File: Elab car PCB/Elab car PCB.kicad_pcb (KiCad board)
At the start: 2 copper layers, 0 parts

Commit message: PCB creation
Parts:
- added C1: 20pF, Capacitor_SMD:C_1206_3216Metric_Pad1.33x1.80mm_HandSolder, F.Cu at (182.2, 73.7)
- added C2: 20pF, Capacitor_SMD:C_1206_3216Metric_Pad1.33x1.80mm_HandSolder, F.Cu at (193.7, 73.7)
- added C3: 10µF, Capacitor_SMD:CP_Elec_5x4.5, F.Cu at (114.9, 89.5)
- added C4: 22µF, Capacitor_SMD:CP_Elec_5x5.3, F.Cu at (94.6, 89.5)
- added C5: 47µF, Capacitor_SMD:CP_Elec_6.3x5.8, F.Cu at (104.1, 130.2)
- added C6: 10µF, Capacitor_SMD:CP_Elec_5x4.5, F.Cu at (104.5, 105.4)
- added C7: 100nF, Capacitor_SMD:C_1206_3216Metric_Pad1.33x1.80mm_HandSolder, F.Cu at (121.3, 51.8)
- added D1: D_Schottky, Diode_SMD:D_1206_3216Metric_Pad1.42x1.75mm_HandSolder, F.Cu at (183.5, 101.0)
- added D10: D_Schottky, Diode_SMD:D_1206_3216Metric_Pad1.42x1.75mm_HandSolder, F.Cu at (163.0, 89.7)
- added D11: WS2812B, LED_SMD:LED_WS2812B_PLCC4_5.0x5.0mm_P3.2mm, F.Cu at (95.5, 61.3)
- added D12: WS2812B, LED_SMD:LED_WS2812B_PLCC4_5.0x5.0mm_P3.2mm, F.Cu at (95.5, 141.9)
- added D13: WS2812B, LED_SMD:LED_WS2812B_PLCC4_5.0x5.0mm_P3.2mm, F.Cu at (183.9, 141.9)
- added D14: WS2812B, LED_SMD:LED_WS2812B_PLCC4_5.0x5.0mm_P3.2mm, F.Cu at (183.9, 61.3)
- added D15: Blue_led, LED_SMD:LED_0805_2012Metric_Pad1.15x1.40mm_HandSolder, F.Cu at (137.8, 73.4)
- added D16: D_Schottky, Diode_SMD:D_1206_3216Metric_Pad1.42x1.75mm_HandSolder, F.Cu at (113.7, 116.8)
- added D17: 3.3V PWR, LED_SMD:LED_0805_2012Metric_Pad1.15x1.40mm_HandSolder, F.Cu at (85.0, 98.0)
- added D18: D_Schottky, Diode_SMD:D_1206_3216Metric_Pad1.42x1.75mm_HandSolder, F.Cu at (112.4, 111.8)
- added D19: 5V PWR, LED_SMD:LED_0805_2012Metric_Pad1.15x1.40mm_HandSolder, F.Cu at (85.0, 105.0)
- added D2: D_Schottky, Diode_SMD:D_1206_3216Metric_Pad1.42x1.75mm_HandSolder, F.Cu at (112.8, 121.9)
- added D20: D_Schottky, Diode_SMD:D_1206_3216Metric_Pad1.42x1.75mm_HandSolder, F.Cu at (164.7, 45.1)
- added D3: D_Schottky, Diode_SMD:D_1206_3216Metric_Pad1.42x1.75mm_HandSolder, F.Cu at (153.0, 113.5)
- added D4: D_Schottky, Diode_SMD:D_1206_3216Metric_Pad1.42x1.75mm_HandSolder, F.Cu at (163.0, 121.5)
- added D5: D_Schottky, Diode_SMD:D_1206_3216Metric_Pad1.42x1.75mm_HandSolder, F.Cu at (153.0, 81.7)
- added D6: D_Schottky, Diode_SMD:D_1206_3216Metric_Pad1.42x1.75mm_HandSolder, F.Cu at (163.0, 81.7)
- added D7: D_Schottky, Diode_SMD:D_1206_3216Metric_Pad1.42x1.75mm_HandSolder, F.Cu at (153.0, 121.5)
- added D8: D_Schottky, Diode_SMD:D_1206_3216Metric_Pad1.42x1.75mm_HandSolder, F.Cu at (163.0, 113.5)
- added D9: D_Schottky, Diode_SMD:D_1206_3216Metric_Pad1.42x1.75mm_HandSolder, F.Cu at (153.0, 89.7)
- added F1: 500mA, Fuse:Fuse_1206_3216Metric_Pad1.42x1.75mm_HandSolder, F.Cu at (189.9, 101.0)
- added J1: USB_B, Connector_USB:USB_B_Lumberg_2411_02_Horizontal, F.Cu at (195.2, 101.0)
- added J10: Conn_01x04, Connector_PinHeader_2.54mm:PinHeader_1x04_P2.54mm_Vertical, F.Cu at (114.9, 131.4)
- added J11: Screw_Terminal_01x02, TerminalBlock:TerminalBlock_bornier-2_P5.08mm, F.Cu at (193.7, 116.8)
- added J12: Screw_Terminal_01x02, TerminalBlock:TerminalBlock_bornier-2_P5.08mm, F.Cu at (179.1, 116.8)
- added J2: Screw_Terminal_01x02, TerminalBlock:TerminalBlock_bornier-2_P5.08mm, F.Cu at (123.6, 99.0)
- added J3: Screw_Terminal_01x02, TerminalBlock:TerminalBlock_bornier-2_P5.08mm, F.Cu at (137.2, 117.5)
- added J4: Screw_Terminal_01x02, TerminalBlock:TerminalBlock_bornier-2_P5.08mm, F.Cu at (142.2, 85.7)
- added J5: Conn_01x04, Connector_PinHeader_2.54mm:PinHeader_1x04_P2.54mm_Vertical, F.Cu at (135.9, 131.4)
- added J6: Conn_01x03, Connector_PinHeader_2.54mm:PinHeader_1x03_P2.54mm_Vertical, F.Cu at (124.4, 160.0)
- added J7: Conn_01x03, Connector_PinHeader_2.54mm:PinHeader_1x03_P2.54mm_Vertical, F.Cu at (155.0, 160.0)
- added J8: Conn_01x03, Connector_PinHeader_2.54mm:PinHeader_1x03_P2.54mm_Vertical, F.Cu at (130.2, 79.4)
- added J9: Conn_01x08, Connector_PinHeader_2.54mm:PinHeader_1x08_P2.54mm_Vertical, F.Cu at (171.4, 131.4)
- added Q1: S8050, Package_TO_SOT_SMD:SOT-23_Handsoldering, F.Cu at (162.6, 50.8)
- added Q2: S8050, Package_TO_SOT_SMD:SOT-23_Handsoldering, F.Cu at (169.2, 50.6)
- added Q3: 2N7000, Package_TO_SOT_THT:TO-92_Inline, F.Cu at (177.8, 130.2)
- added Q4: 2N7000, Package_TO_SOT_THT:TO-92_Inline, F.Cu at (187.3, 130.2)
- added R1: 85R, Resistor_SMD:R_1206_3216Metric_Pad1.30x1.75mm_HandSolder, F.Cu at (142.9, 73.3)
- added R11: 12k, Resistor_SMD:R_1206_3216Metric_Pad1.30x1.75mm_HandSolder, F.Cu at (148.0, 73.3)
- added R12: 12k, Resistor_SMD:R_1206_3216Metric_Pad1.30x1.75mm_HandSolder, F.Cu at (179.4, 124.5)
- added R13: 12k, Resistor_SMD:R_1206_3216Metric_Pad1.30x1.75mm_HandSolder, F.Cu at (187.0, 124.5)
- added R2: 12k, Resistor_SMD:R_1206_3216Metric_Pad1.30x1.75mm_HandSolder, F.Cu at (126.4, 51.8)
- added R3: 12k, Resistor_SMD:R_1206_3216Metric_Pad1.30x1.75mm_HandSolder, F.Cu at (121.3, 66.7)
- added R4: 12k, Resistor_SMD:R_1206_3216Metric_Pad1.30x1.75mm_HandSolder, F.Cu at (121.3, 77.8)
- added R5: 20R, Resistor_SMD:R_1206_3216Metric_Pad1.30x1.75mm_HandSolder, F.Cu at (92.0, 98.0)
- added R6: 85r, Resistor_SMD:R_1206_3216Metric_Pad1.30x1.75mm_HandSolder, F.Cu at (92.0, 105.0)
- added R7: 12k, Resistor_SMD:R_1206_3216Metric_Pad1.30x1.75mm_HandSolder, F.Cu at (166.0, 55.9)
- added R8: 12k, Resistor_SMD:R_1206_3216Metric_Pad1.30x1.75mm_HandSolder, F.Cu at (166.1, 61.0)
- added SW1: SW_Push, Button_Switch_THT:SW_PUSH_6mm_H5mm, F.Cu at (109.7, 48.9)
- added SW2: SW_Push, Button_Switch_THT:SW_PUSH_6mm_H5mm, F.Cu at (109.7, 64.1)
- added SW3: SW_Push, Button_Switch_THT:SW_PUSH_6mm_H5mm, F.Cu at (109.7, 74.9)
- added U1: CH340G, Package_SO:SOIC-16_3.9x9.9mm_P1.27mm, F.Cu at (191.8, 85.7)
- added U2: L293D, Package_DIP:DIP-16_W7.62mm, F.Cu at (154.7, 105.4)
- added U3: AMS1117-3.3, Package_TO_SOT_SMD:SOT-223-3_TabPin2, F.Cu at (104.8, 89.5)
- added U4: ESP32-WROOM-32, RF_Module:ESP32-WROOM-32, F.Cu at (139.7, 56.6)
- added U5: L7805, Package_TO_SOT_SMD:TO-263-2, F.Cu at (99.7, 116.8)
- added Y1: Crystal_GND24, Crystal:Crystal_SMD_3225-4Pin_3.2x2.5mm_HandSoldering, F.Cu at (188.0, 74.3)
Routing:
- net +5V: track 0.00 -> 509.1 mm
- net +3V3: track 0.00 -> 397.5 mm, vias 0 -> 6
- net mot_pwr: track 0.00 -> 178.9 mm, vias 0 -> 2
- net Net-(D12-Pad2): track 0.00 -> 167.3 mm
- net /line_sens_2: track 0.00 -> 120.6 mm, vias 0 -> 2
- net Net-(D11-Pad2): track 0.00 -> 120.5 mm
- net Net-(D13-Pad2): track 0.00 -> 111.3 mm
- net /line_sens_1: track 0.00 -> 109.3 mm, vias 0 -> 1
- net /esp_SCL: track 0.00 -> 104.5 mm, vias 0 -> 1
- net /SCL: track 0.00 -> 100.5 mm
- net /esp_SDA: track 0.00 -> 97.3 mm, vias 0 -> 1
- net GND: track 0.00 -> 88.6 mm, vias 0 -> 47
- net /SDA: track 0.00 -> 87.6 mm
- net /mot1for: track 0.00 -> 86.5 mm
- net /mot1en: track 0.00 -> 86.3 mm, vias 0 -> 1
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- added copper zone on B.Cu, net GND
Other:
- board outline added: 139.1 x 138.8 mm

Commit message: Silk screen
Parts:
- added TP1: TestPoint, TestPoint:TestPoint_Pad_D2.5mm, F.Cu at (123.2, 112.4)
- added TP10: TestPoint, TestPoint:TestPoint_Pad_D2.5mm, F.Cu at (130.2, 73.7)
- added TP11: TestPoint, TestPoint:TestPoint_Pad_D2.5mm, F.Cu at (147.3, 122.6)
- added TP12: TestPoint, TestPoint:TestPoint_Pad_D2.5mm, F.Cu at (168.9, 117.5)
- added TP13: TestPoint, TestPoint:TestPoint_Pad_D2.5mm, F.Cu at (156.2, 86.4)
- added TP14: TestPoint, TestPoint:TestPoint_Pad_D2.5mm, F.Cu at (158.1, 81.3)
- added TP15: TestPoint, TestPoint:TestPoint_Pad_D2.5mm, F.Cu at (120.0, 72.4)
- added TP16: TestPoint, TestPoint:TestPoint_Pad_D2.5mm, F.Cu at (161.3, 40.6)
- added TP17: TestPoint, TestPoint:TestPoint_Pad_D2.5mm, F.Cu at (173.4, 46.4)
- added TP18: TestPoint, TestPoint:TestPoint_Pad_D2.5mm, F.Cu at (102.9, 52.7)
- added TP19: TestPoint, TestPoint:TestPoint_Pad_D2.5mm, F.Cu at (159.4, 139.1)
- added TP2: TestPoint, TestPoint:TestPoint_Pad_D2.5mm, F.Cu at (198.8, 91.4)
- added TP20: TestPoint, TestPoint:TestPoint_Pad_D2.5mm, F.Cu at (116.2, 141.6)
- added TP21: TestPoint, TestPoint:TestPoint_Pad_D2.5mm, F.Cu at (159.4, 59.1)
- added TP22: TestPoint, TestPoint:TestPoint_Pad_D2.5mm, F.Cu at (156.2, 52.1)
- added TP3: TestPoint, TestPoint:TestPoint_Pad_D2.5mm, F.Cu at (198.1, 81.3)
- added TP4: TestPoint, TestPoint:TestPoint_Pad_D2.5mm, F.Cu at (97.8, 98.4)
- added TP5: TestPoint, TestPoint:TestPoint_Pad_D2.5mm, F.Cu at (112.4, 102.2)
- added TP6: TestPoint, TestPoint:TestPoint_Pad_D2.5mm, F.Cu at (128.3, 122.6)
- added TP7: TestPoint, TestPoint:TestPoint_Pad_D2.5mm, F.Cu at (121.9, 85.1)
- added TP8: TestPoint, TestPoint:TestPoint_Pad_D2.5mm, F.Cu at (102.2, 68.6)
- added TP9: TestPoint, TestPoint:TestPoint_Pad_D2.5mm, F.Cu at (131.4, 113.0)
- D10, D3, D4, D5, D6, D7, D8, D9: value D_Schottky -> Flyback
- D15: value Blue_led -> LED_BUILTIN
- J10: value Conn_01x04 -> I2C
- J11: value Screw_Terminal_01x02 -> SCL pullup
- J12: value Screw_Terminal_01x02 -> SDA pullup
- J2: value Screw_Terminal_01x02 -> Power input
- J3: value Screw_Terminal_01x02 -> L_Mot
- J4: value Screw_Terminal_01x02 -> R_Mot
- J5: value Conn_01x04 -> HC-SR04
- J6: value Conn_01x03 -> R_Line
- J7: value Conn_01x03 -> L_Line
- J8: value Conn_01x03 -> Servo
- J9: value Conn_01x08 -> MPU5060
- SW1: value SW_Push -> Reset
- SW2: value SW_Push -> User 1
- SW3: value SW_Push -> User 2
- Y1: value Crystal_GND24 -> 12MHz
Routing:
- net /esp_SDA: track 97.3 -> 124.6 mm, vias 1 -> 2
- net Net-(D7-Pad2): track 46.8 -> 60.2 mm
- net Net-(D20-Pad1): track 6.59 -> 17.7 mm, vias 0 -> 2
- net /SCL: track 100.5 -> 111.2 mm, vias 0 -> 1
- net /SDA: track 87.6 -> 98.2 mm
- net /BP_2: track 41.1 -> 49.7 mm
- net /BP_1: track 32.3 -> 39.8 mm
- net /esp_EN: track 57.3 -> 64.4 mm
- net /line_sens_2: track 120.6 -> 127.5 mm, vias 2 -> 3
- net Net-(D3-Pad2): track 55.8 -> 62.5 mm
- net /servo_sig: track 25.5 -> 31.5 mm
- net /line_sens_1: track 109.3 -> 115.3 mm
- net /esp_SCL: track 104.5 -> 110.1 mm
- net /esp_IO0: track 56.9 -> 61.9 mm
- net /D+: track 32.6 -> 37.5 mm
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- added copper zone on F.Cu, net GND
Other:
- board text added: "+"
- board text added: "-"
- board text added: "I²C"
- board text added: "Motors control"
- board text added: "Power management"
- board text added: "Sensors"
- board text added: "USB Management"
- board text added: "electroLABOT V1.0 Yann Jacquet - electroLAB - Umons 2021-09-21"

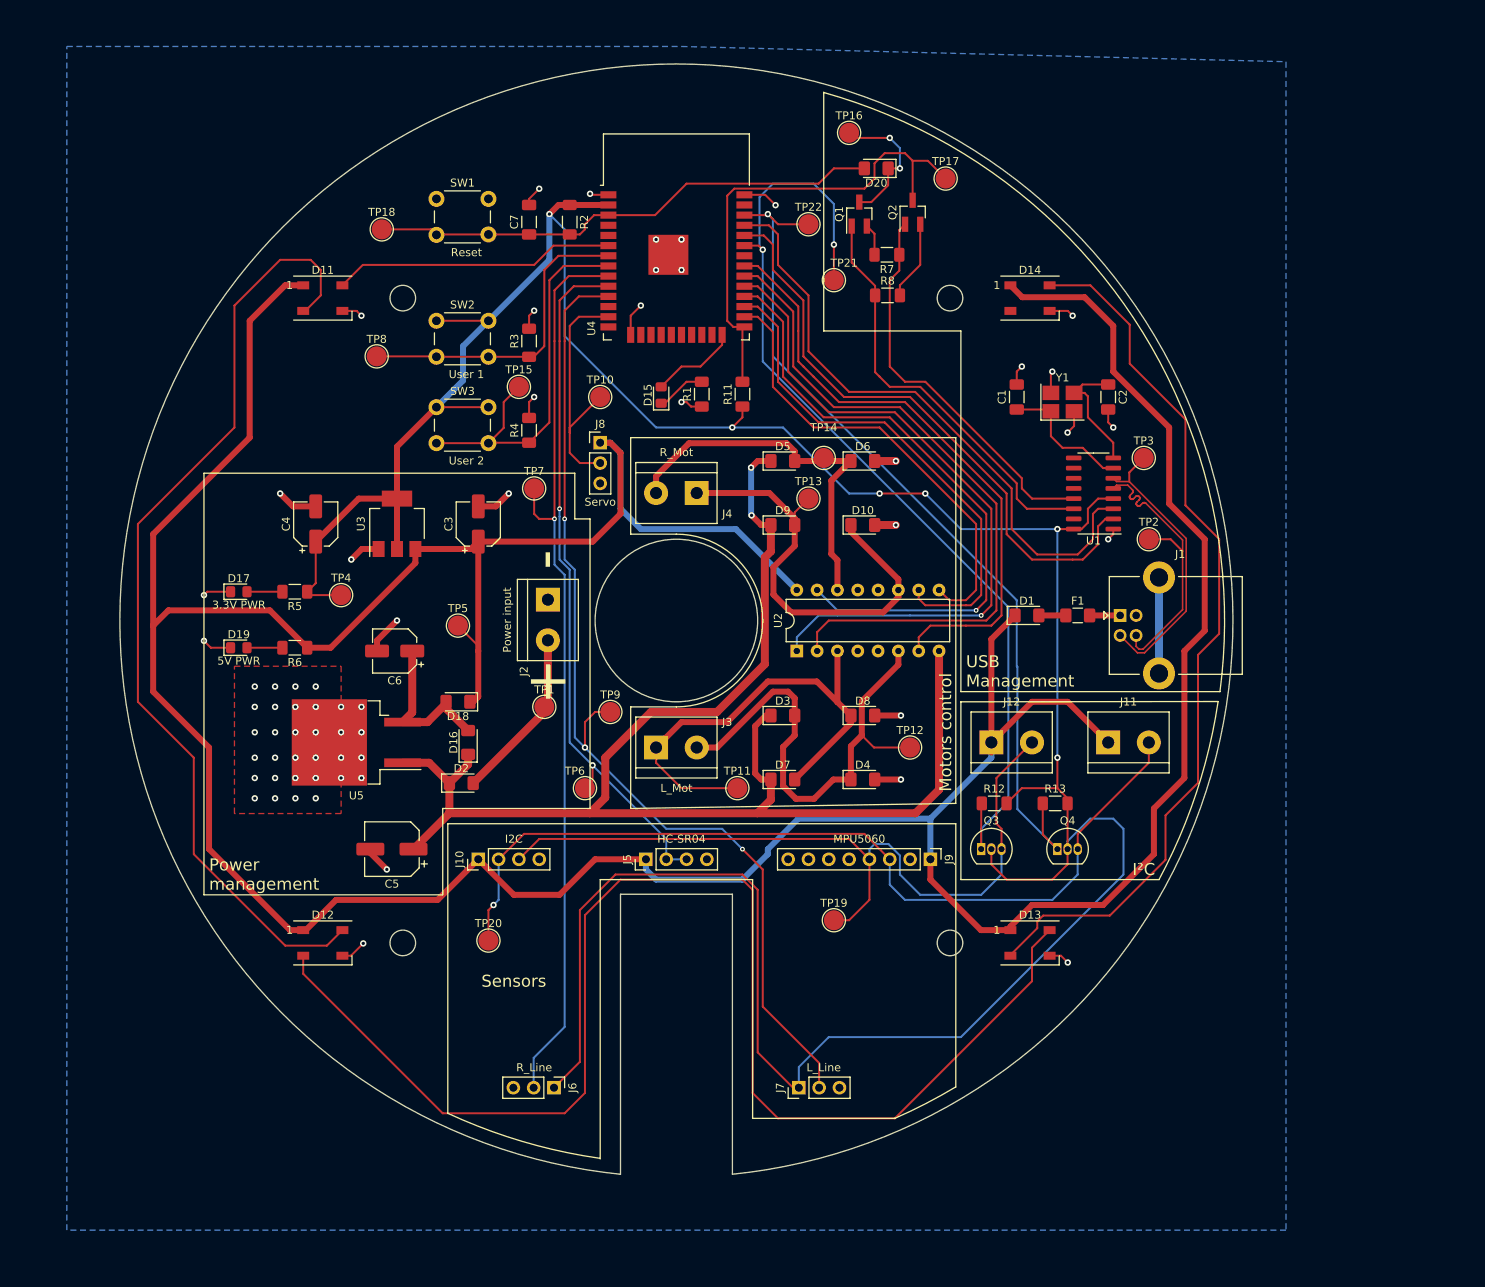
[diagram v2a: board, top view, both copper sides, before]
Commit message: Esp32 design requirements corrections
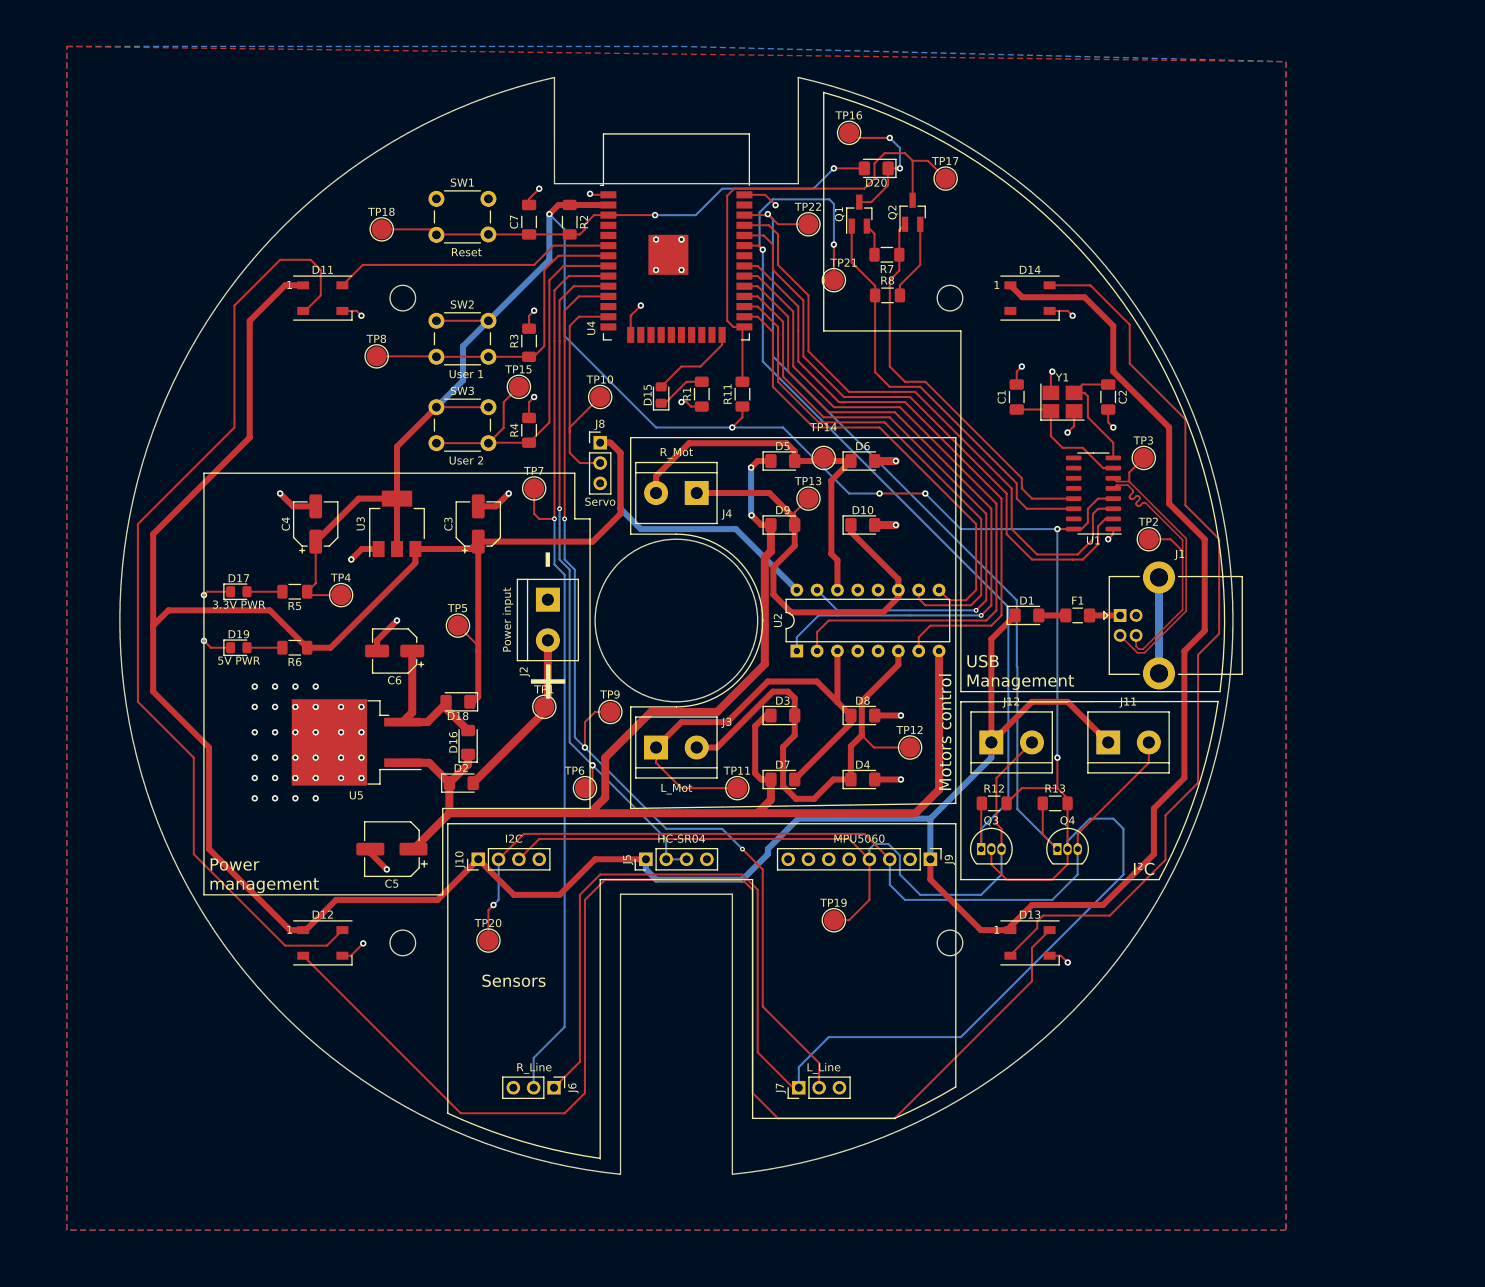
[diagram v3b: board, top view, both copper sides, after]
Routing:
- net /esp_SDA: track 124.6 -> 121.8 mm
- net +3V3: track 401.9 -> 403.0 mm
- net /esp_EN: vias 0 -> 2
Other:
- board size 139.1 x 138.8 mm -> 139.1 x 137.1 mm
- board text added: "electroLABOT V1.0 Yann Jacquet - electroLAB - UMONS 2021-09-21"
- board text removed: "electroLABOT V1.0 Yann Jacquet - electroLAB - Umons 2021-09-21"

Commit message: Board edge adjustment
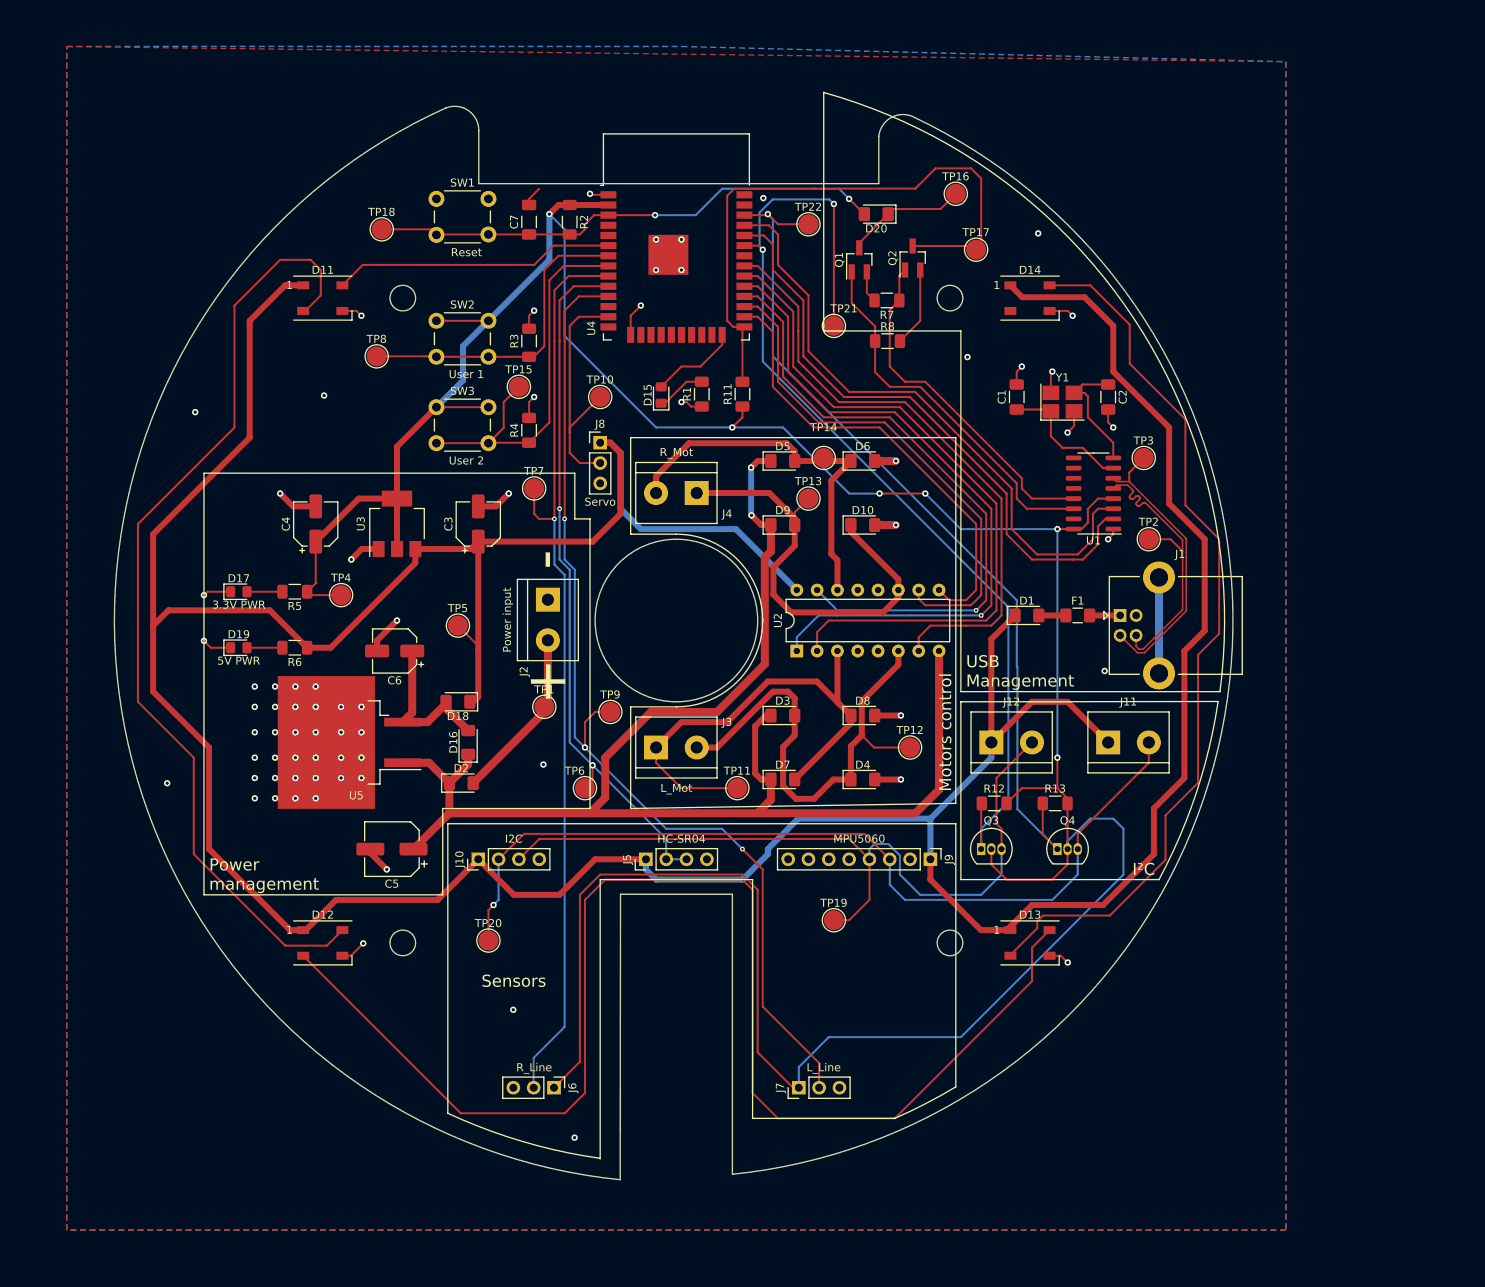
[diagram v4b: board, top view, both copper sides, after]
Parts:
- moved TP16 15.4 mm to (174.6, 48.3)
- moved TP17 9.67 mm to (177.2, 55.2)
- moved Q1 5.72 mm to (162.6, 56.5)
- moved D20 5.71 mm to (164.7, 50.8)
- moved Q2 5.71 mm to (169.2, 56.3)
- moved R7 5.71 mm to (166.0, 61.6)
- moved R8 5.71 mm to (166.1, 66.7)
- moved TP21 5.71 mm to (159.4, 64.8)
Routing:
- net /esp_IO0: track 61.9 -> 76.0 mm
- net /DTR: track 49.1 -> 43.4 mm
- net /RTS: track 52.5 -> 46.8 mm
- net /esp_SDA: track 121.8 -> 127.6 mm
- net GND: track 86.4 -> 82.0 mm, vias 63 -> 71
- net Net-(D20-Pad1): track 17.7 -> 15.2 mm, vias 2 -> 0
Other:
- board size 139.1 x 137.1 mm -> 139.8 x 134.2 mm
